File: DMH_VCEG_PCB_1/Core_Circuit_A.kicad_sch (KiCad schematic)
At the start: 104 parts, among them J21 Conn_01x10_PinHeader, J22 Conn_01x10_PinHeader, J24 Conn_01x06_PinHeader, Q1 BC558, Q10 BC548, Q2 BC558, Q3 BC548, Q4 BC548, Q5 MMBFJ113, Q6 MMBFJ113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

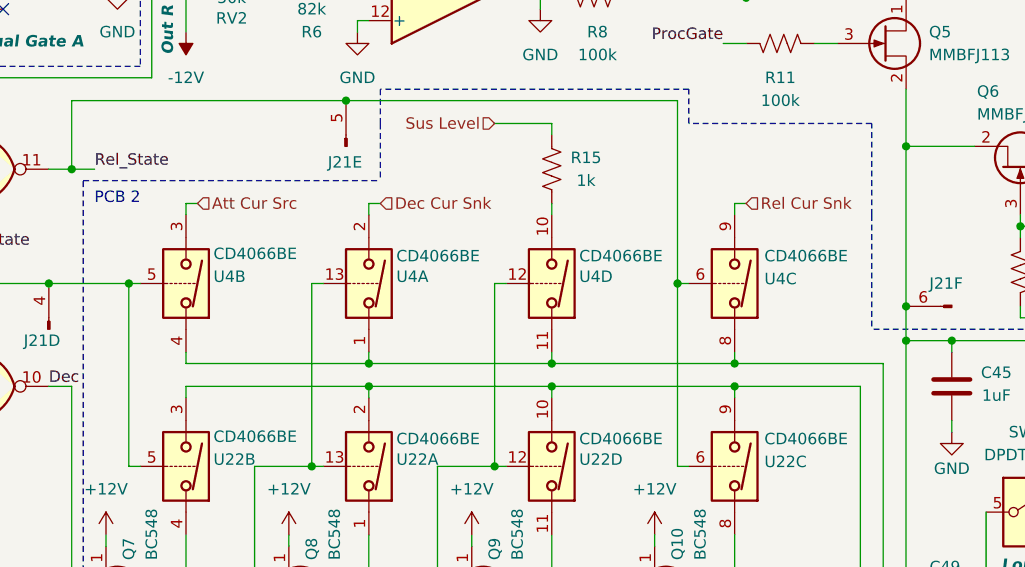
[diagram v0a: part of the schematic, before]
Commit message: Small changes during breadboarding
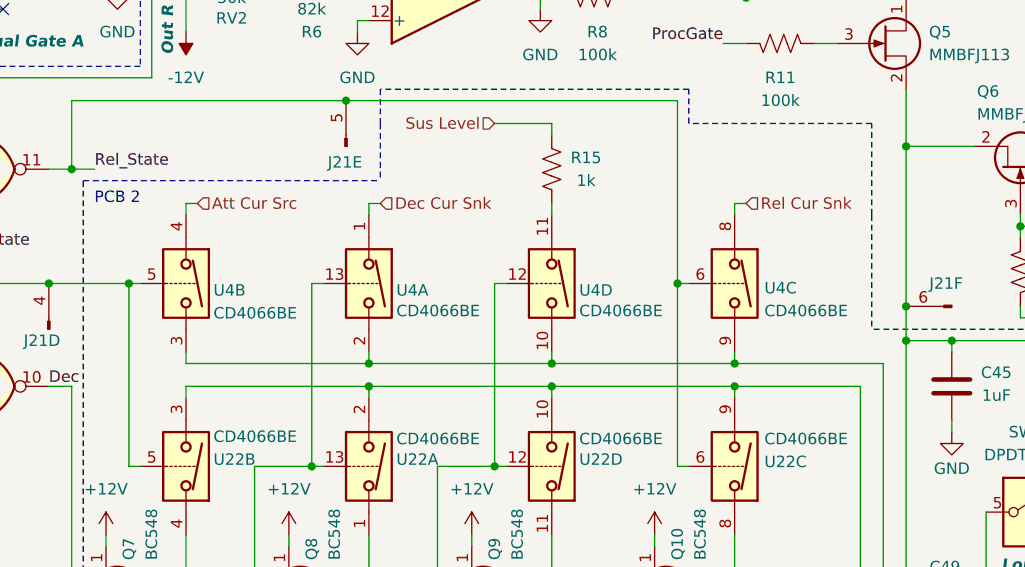
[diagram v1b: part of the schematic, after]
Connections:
- net Att Cur Src: now also U4.4; no longer U4.3
- net Dec Cur Snk: now also U4.1; no longer U4.2
- net Rel Cur Snk: now also U4.8; no longer U4.9
- net at C50.1, C51.1, J21.7 (Pin_7)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: now also U4.10, U4.2, U4.3, U4.9; no longer U4.1, U4.11, U4.4, U4.8
- net at R15.1: now also U4.11; no longer U4.10
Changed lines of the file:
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@@
 		(lib_id "Analog_Switch:CD4066BE")
 		(at 201.93 63.5 270)
-		(mirror x)
 		(unit 4)
 		(exclude_from_sim no)
@@
 		(dnp no)
 		(property "Reference" "U4"
-			(at 204.978 62.738 90)
+			(at 204.978 64.262 90)
 			(effects
 				(font
@@
 		)
 		(property "Value" "CD4066BE"
-			(at 204.978 60.452 90)
+			(at 204.978 66.548 90)
 			(effects
 				(font
@@
 		(lib_id "Analog_Switch:CD4066BE")
 		(at 181.61 63.5 270)
-		(mirror x)
 		(unit 1)
 		(exclude_from_sim no)
@@
 		(dnp no)
 		(property "Reference" "U4"
-			(at 184.658 62.738 90)
+			(at 184.658 64.262 90)
 			(effects
 				(font
@@
 		)
 		(property "Value" "CD4066BE"
-			(at 184.658 60.4521 90)
+			(at 184.658 66.5479 90)
 			(effects
 				(font
@@
 		(lib_id "Analog_Switch:CD4066BE")
 		(at 222.25 63.5 270)
-		(mirror x)
 		(unit 3)
 		(exclude_from_sim no)
@@
 		(dnp no)
 		(property "Reference" "U4"
-			(at 225.552 62.992 90)
+			(at 225.552 64.008 90)
 			(effects
 				(font
@@
 		)
 		(property "Value" "CD4066BE"
-			(at 225.552 60.452 90)
+			(at 225.552 66.548 90)
 			(effects
 				(font
@@
 		(lib_id "Analog_Switch:CD4066BE")
 		(at 161.29 63.5 270)
-		(mirror x)
 		(unit 2)
 		(exclude_from_sim no)
@@
 		(dnp no)
 		(property "Reference" "U4"
-			(at 164.338 62.738 90)
+			(at 164.338 64.262 90)
 			(effects
 				(font
@@
 		)
 		(property "Value" "CD4066BE"
-			(at 164.338 60.198 90)
+			(at 164.338 66.802 90)
 			(effects
 				(font

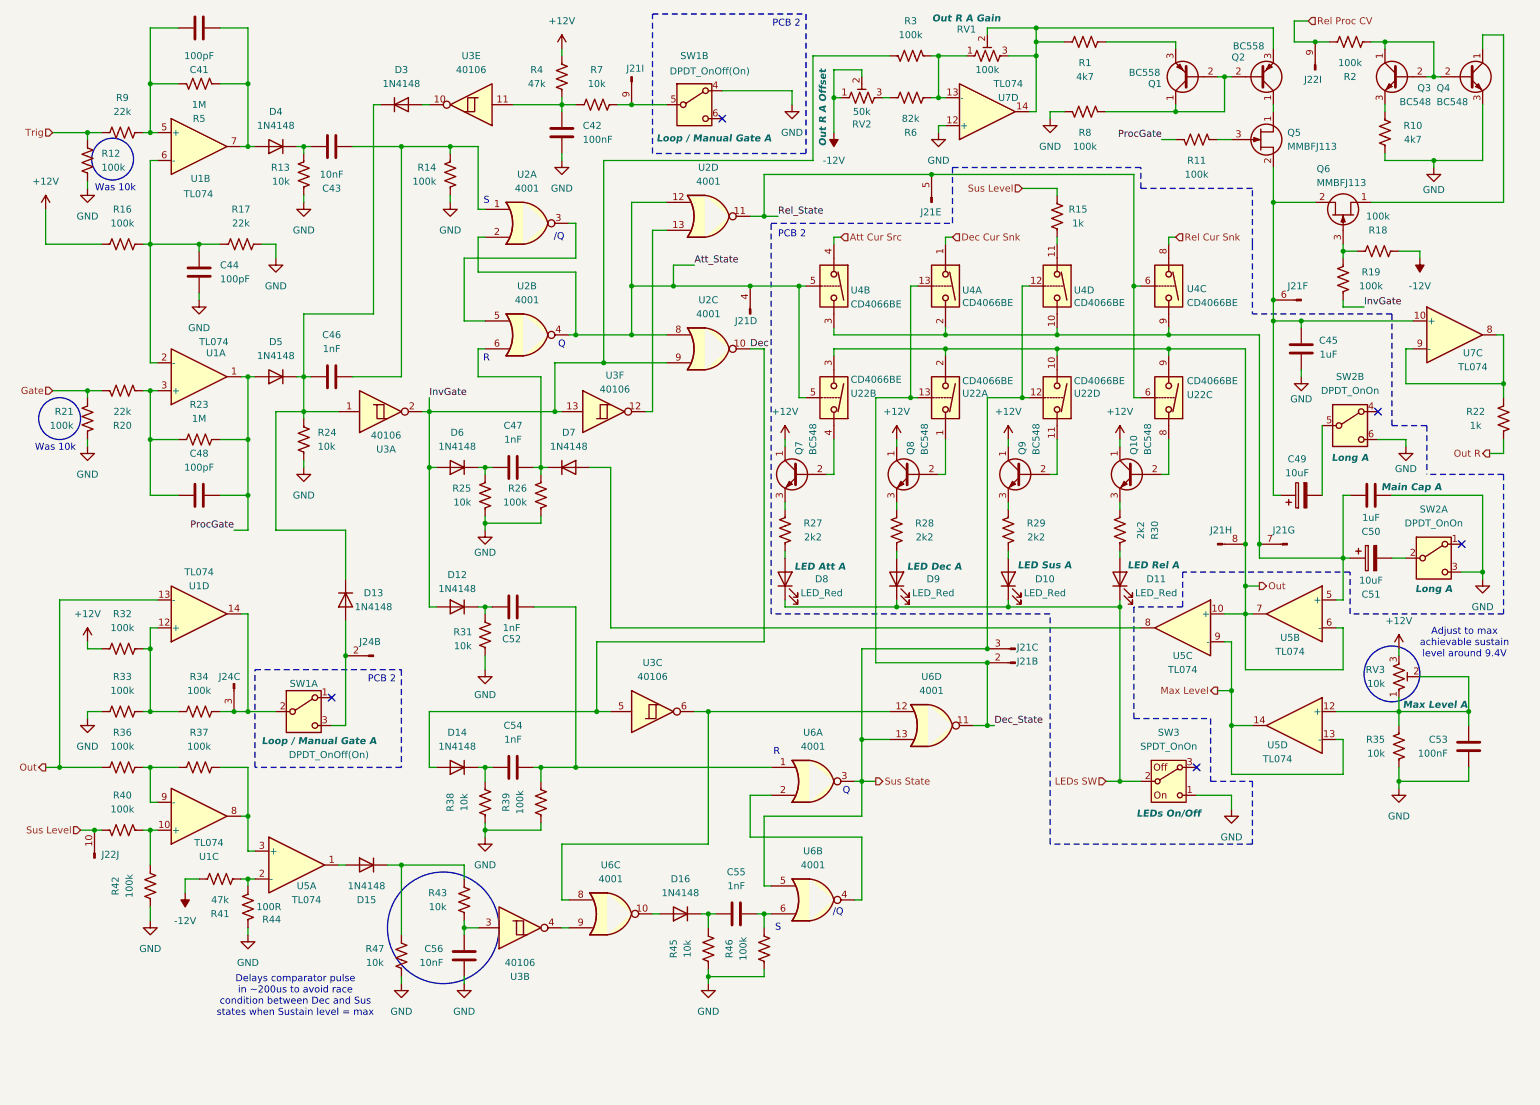
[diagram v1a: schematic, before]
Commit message: Mods on PCB 1 after breadboarding
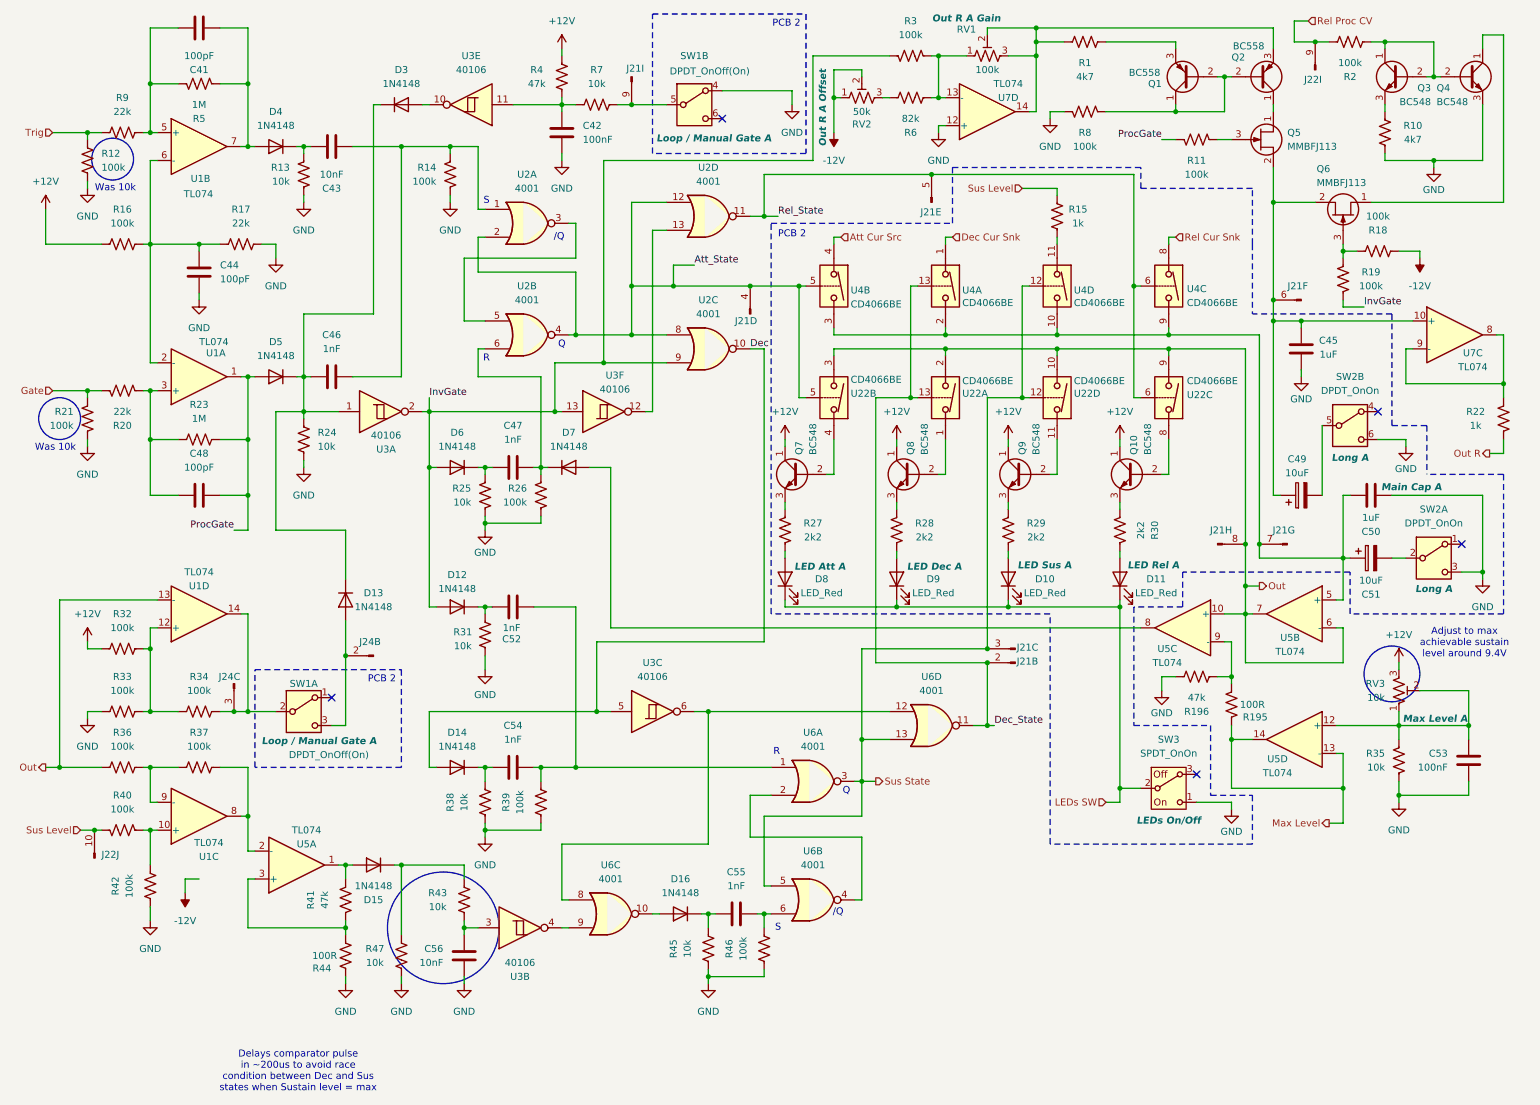
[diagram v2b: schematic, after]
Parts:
- added R195: 100R, Resistor_THT:R_Axial_DIN0207_L6.3mm_D2.5mm_P7.62mm_Horizontal, symbol Device:R_US
- added R196: 47k, Resistor_THT:R_Axial_DIN0207_L6.3mm_D2.5mm_P7.62mm_Horizontal, symbol Device:R_US
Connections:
- net -12V: no longer R41.1
- net GND: now also R196.1
- net Max Level: now also R195.2; no longer U5.9 (-)
- net at R37.1, U1.8: now also U5.2 (-); no longer U5.3 (+)
- net at D15.2 (A), U5.1: now also R41.2
- new net: R195.1, R196.2, U5.9 (-)
- new net: R41.1, R44.1, U5.3 (+)
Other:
- moved on the sheet: C53, D15, R35, R41, R44, RV3, SW3, U5D

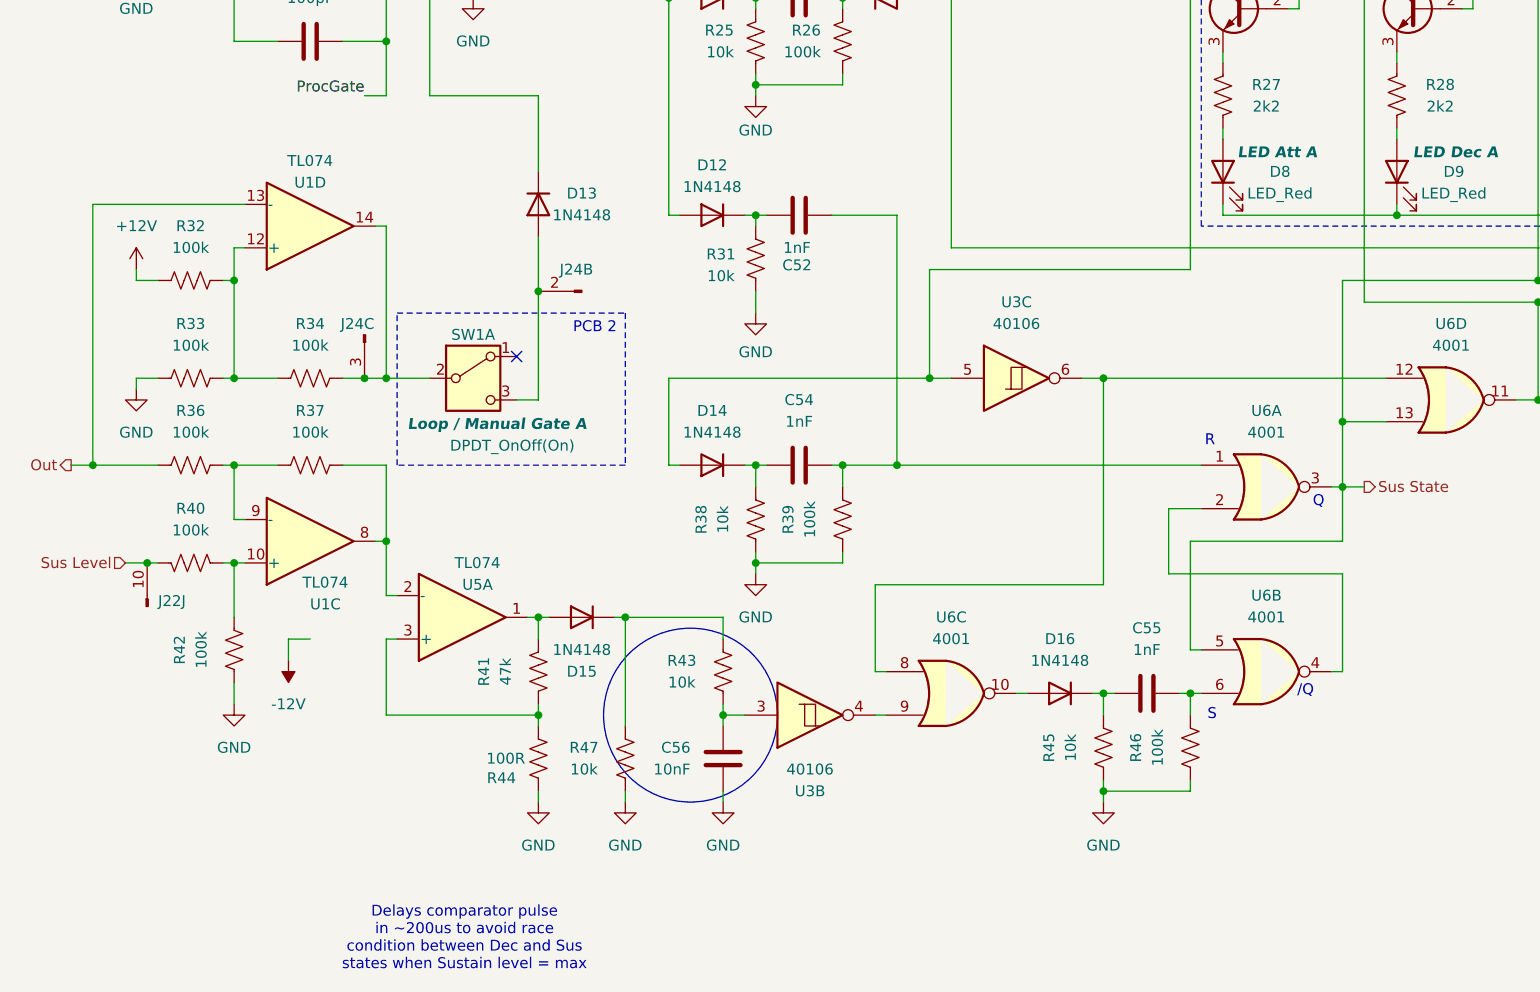
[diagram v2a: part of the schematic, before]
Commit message: Fixed sus state detection circuit A
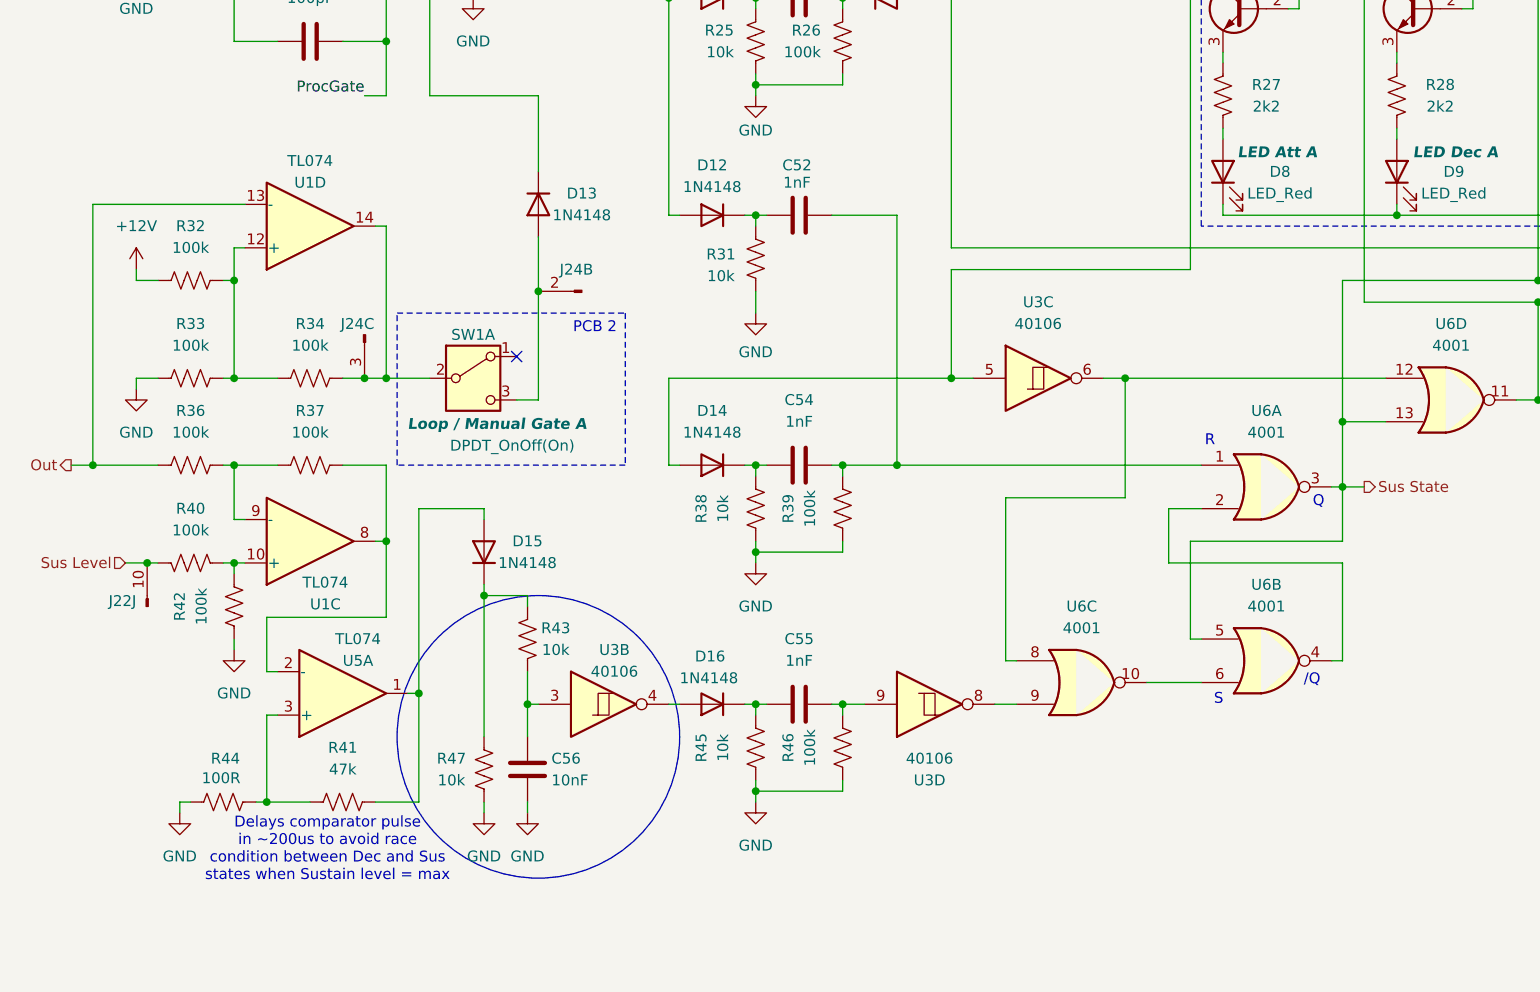
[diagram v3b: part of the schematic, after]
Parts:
- added unit 4 of U3
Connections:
- net GND: now also R44.1; no longer R44.2
- net at U6.10: now also U6.6; no longer D16.2 (A)
- net at U6.9: now also U3.8; no longer U3.4
- net at C55.2, R46.1: now also U3.9; no longer U6.6
- net at D15.2 (A), U5.1: now also R41.1; no longer R41.2
- new net: D16.2 (A), U3.4
- new net: R41.2, R44.2, U5.3 (+)
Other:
- moved on the sheet: C55, C56, D15, D16, J22J, R38, R39, R41, R42, R43, R44, R45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

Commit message: Update Core_Circuit_A.kicad_sch
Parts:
- C43: value 10nF -> 1nF
- R32: value 100k -> 51k
- R34: value 100k -> 47k
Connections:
- net at J24.2 (Pin_2), SW1.3 (C): now also C46.1, D3.1 (K), D5.1 (K), R24.2, U3.1; no longer D13.2 (A)
- net at J24.3 (Pin_3), SW1.2 (B): now also D13.1 (K); no longer R34.1, U1.14
- new net: D13.2 (A), R34.1, U1.14
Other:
- note added: "Was 10n"
- moved on the sheet: D13, J24B, SW1A
